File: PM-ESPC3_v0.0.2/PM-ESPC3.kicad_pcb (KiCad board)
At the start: 2 copper layers, 30.5 x 55.9 mm, 15 parts, among them J1 U254-051T-4BH83-S1S, J2 PinHeader_01x13_P2.54_THT_str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, J3 PinHeader_01x01_P2.54_THT_str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, SW1 Button, SW2 Button, SW3 DIP_SW-3P-P2.54-THT-Top, U1 ESP32-C3-WROOM-02U-N4

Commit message: new PM-RQ8
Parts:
- added C4: 10uF, Capacitor_SMD:C_1206_3216Metric_Pad1.33x1.80mm_HandSolder, F.Cu at (85.2, 133.0)
- added C5: 22uF, Capacitor_SMD:C_1206_3216Metric_Pad1.33x1.80mm_HandSolder, F.Cu at (85.2, 122.9)
- added D1: B5819W, Diode_SMD:D_SOD-123, F.Cu at (75.0, 128.0)
- added D2: B5819W, Diode_SMD:D_SOD-123, F.Cu at (75.0, 133.0)
- added D3: 5A 9.8V 6V, Diode_SMD:D_SOD-323_HandSoldering, F.Cu at (80.1, 133.0)
- added D4: Green, LED_SMD:LED_1206_3216Metric_Pad1.42x1.75mm_HandSolder, F.Cu at (75.0, 122.9)
- added H1: MountingHole, MountingHole:MountingHole_2.2mm_M2, F.Cu at (87.0, 139.0)
- added H2: MountingHole, MountingHole:MountingHole_2.2mm_M2, F.Cu at (53.0, 147.0)
- added H3: MountingHole, MountingHole:MountingHole_2.2mm_M2, F.Cu at (87.0, 61.0)
- added H4: MountingHole, MountingHole:MountingHole_2.2mm_M2, F.Cu at (53.0, 53.0)
- added J4: R-RJ11R04P-A802, kicad_inventree_lib:R-RJ11R04P-A802, F.Cu at (62.0, 148.0)
- added J5: X10B25L08T, kicad_inventree_lib:X10B25L08T, F.Cu at (67.5, 70.0)
- added J6: X10B25L08T, kicad_inventree_lib:X10B25L08T, F.Cu at (67.5, 90.0)
- added J7: X10B25L08T, kicad_inventree_lib:X10B25L08T, F.Cu at (67.5, 130.0)
- added R5: 680R, Resistor_SMD:R_1206_3216Metric_Pad1.30x1.75mm_HandSolder, F.Cu at (80.1, 125.4)
- added U2: CJA1117B-3.3, Package_TO_SOT_SMD:SOT-89-3, F.Cu at (85.2, 127.9)
- J2: value PinHeader_01x13_P2.54_THT_straight -> X10B25L08T; footprint Connector_PinHeader_2.54mm:PinHeader_1x13_P2.54mm_Vertical -> kicad_inventree_lib:X10B25L08T; moved to F.Cu
- J3: value PinHeader_01x01_P2.54_THT_straight -> R-RJ11R04P-A802; footprint Connector_PinHeader_2.54mm:PinHeader_1x01_P2.54mm_Vertical -> kicad_inventree_lib:R-RJ11R04P-A802; moved to F.Cu
- SW3: moved to F.Cu
- moved J3 77.7 mm to (75.0, 148.0)
- moved SW2 60.0 mm to (87.7, 67.0), turned to -90 degrees
- moved SW1 56.1 mm to (82.6, 67.0), turned to -90 degrees
- moved C3 45.8 mm to (87.7, 77.1), turned to 90 degrees
- moved R4 42.7 mm to (72.5, 77.1), turned to 90 degrees
- moved C1 37.7 mm to (82.6, 77.1), turned to 90 degrees
- moved R8 36.8 mm to (87.7, 115.2), turned to 90 degrees
- moved C2 36.6 mm to (87.7, 84.8)
- moved R3 32.6 mm to (72.5, 84.8)
- moved J2 32.2 mm to (67.5, 110.0), turned to -90 degrees
- moved R1 31.7 mm to (82.6, 84.8)
- moved R2 29.8 mm to (77.5, 84.8), turned to -90 degrees
- moved J1 26.6 mm to (63.6, 55.1)
- moved SW3 18.3 mm to (71.2, 53.0), turned to 0 degrees
- moved U1 4.40 mm to (82.6, 100.0), turned to -90 degrees
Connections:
- C2 pad 2: /+3.3V -> +3.3V
- C3 pad 1: /+3.3V -> +3.3V
- J1 pad 1: unconnected-(J1-VBUS-Pad1) -> Net-(D1-A)
- J2 pad 1: unconnected-(J2-Pin_1-Pad1) -> +5V
- J2 pad 2: /GPIO2 -> +3.3V
- J2 pad 3: /GPIO3 -> unconnected-(J2-Pin_3-Pad3)
- J2 pad 4: /GPIO9 -> /MOSI
- J2 pad 5: /GPIO8 -> /MISO
- J2 pad 6: /GPIO7 -> /SCK
- J2 pad 7: /GPIO6 -> /CS2
- J2 pad 8: /GPIO5 -> GND
- J3 pad 1: GND -> Net-(D2-A)
- R1 pad 1: /+3.3V -> +3.3V
- R2 pad 1: /+3.3V -> +3.3V
- R2 pad 2: /GPIO8 -> /A1
- R3 pad 1: /+3.3V -> +3.3V
- R3 pad 2: /GPIO9 -> /A2
- R4 pad 1: /GPIO9 -> /A2
- R8 pad 1: /+3.3V -> +3.3V
- R8 pad 2: /GPIO2 -> /MISO
- SW3 pad 1: /A2 -> +3.3V
- SW3 pad 2: /A1 -> +3.3V
- SW3 pad 3: /A0 -> +3.3V
- SW3 pad 4: /+3.3V -> /A0
- SW3 pad 5: /+3.3V -> /A1
- SW3 pad 6: /+3.3V -> /A2
- U1 pad 1: /+3.3V -> +3.3V
- U1 pad 10: /A2 -> /CS0
- U1 pad 11: /A1 -> /CS1
- U1 pad 12: /A0 -> /CS2
- U1 pad 15: /GPIO3 -> /CS3
- U1 pad 16: /GPIO2 -> /MISO
- U1 pad 3: /GPIO4 -> unconnected-(U1-IO4-Pad3)
- U1 pad 4: /GPIO5 -> /MOSI
- U1 pad 5: /GPIO6 -> /SCK
- U1 pad 6: /GPIO7 -> /A0
- U1 pad 7: /GPIO8 -> /A1
- U1 pad 8: /GPIO9 -> /A2
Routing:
- net GND: track 19.9 -> 0.00 mm
- net /USB_D+: track 17.7 -> 0.00 mm
- net /USB_D-: track 17.6 -> 0.00 mm
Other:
- board size 30.5 x 55.9 mm -> 39.8 x 99.8 mm
- board text added: "1"
- board text added: "2"
- board text added: "4"
- board text added: "OFF"
- board text added: "ON"
- board text added: "SPI0"
- board text added: "SPI1"
- board text added: "SPI2"
- board text added: "SPI3"
- board text removed: "+3.3V"
- board text removed: "CS1"
- board text removed: "CS2"
- board text removed: "GND"
- board text removed: "GPIO4"
- board text removed: "GPIO5"
- board text removed: "GPIO6"
- board text removed: "MISO"
- board text removed: "MOSI"
- board text removed: "SCK"
- board text removed: "SCL"
- board text removed: "SDA"

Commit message: update
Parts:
- removed D4: Green, LED_SMD:LED_1206_3216Metric_Pad1.42x1.75mm_HandSolder
- removed J7: X10B25L08T, kicad_inventree_lib:X10B25L08T
- removed R5: 680R, Resistor_SMD:R_1206_3216Metric_Pad1.30x1.75mm_HandSolder
- added J8: AFA07-S10FCC-00, kicad_inventree_lib:CONN10_AFA07-S10_JUS, F.Cu at (63.0, 70.0)
- added R6: 10k, Resistor_SMD:R_1206_3216Metric_Pad1.30x1.75mm_HandSolder, F.Cu at (74.5, 66.0)
- added R7: 330R, Resistor_SMD:R_1206_3216Metric_Pad1.30x1.75mm_HandSolder, F.Cu at (72.5, 115.2)
- J2, J5, J6: value X10B25L08T -> AFA07-S10FCC-00; footprint kicad_inventree_lib:X10B25L08T -> kicad_inventree_lib:CONN10_AFA07-S10_JUS
- moved J6 40.2 mm to (63.0, 130.0)
- moved J5 20.5 mm to (63.0, 90.0)
- moved J2 4.47 mm to (63.0, 110.0)
- moved J4 0.50 mm to (61.7, 147.6)
- moved J3 0.38 mm to (75.0, 147.6)
- moved J1 0.37 mm to (63.8, 55.4)
- moved U1 0.30 mm to (82.3, 100.1)
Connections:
- J2 pad 4: /MOSI -> unconnected-(J2-Pin_4-Pad4)
- J2 pad 5: /MISO -> unconnected-(J2-Pin_5-Pad5)
- J2 pad 6: /SCK -> unconnected-(J2-Pin_6-Pad6)
- J2 pad 7: /CS2 -> unconnected-(J2-Pin_7-Pad7)
- J2 pad 8: GND -> unconnected-(J2-Pin_8-Pad8)
- J5 pad 1: +5V -> unconnected-(J5-Pin_1-Pad1)
- J5 pad 2: +3.3V -> Net-(J5-Pin_2)
- J5 pad 3: unconnected-(J5-Pin_3-Pad3) -> +3.3V
- J5 pad 4: /MOSI -> /LED0
- J5 pad 5: /MISO -> /LED1
- J5 pad 6: /SCK -> /LED2
- J5 pad 7: /CS0 -> /LED3
- J5 pad 8: GND -> unconnected-(J5-Pin_8-Pad8)
- J6 pad 4: /MOSI -> unconnected-(J6-Pin_4-Pad4)
- J6 pad 5: /MISO -> /MOSI
- J6 pad 6: /SCK -> /MISO
- J6 pad 7: /CS1 -> /SCK
- J6 pad 8: GND -> /CS1
- R2 pad 2: /A1 -> /MISO
- R3 pad 2: /A2 -> /CS0
- R4 pad 1: /A2 -> /CS0
- R8 pad 2: /MISO -> /CS1
- SW3 pad 1: +3.3V -> Net-(R6-Pad2)
- SW3 pad 2: +3.3V -> Net-(R6-Pad2)
- SW3 pad 3: +3.3V -> Net-(R6-Pad2)
- SW3 pad 4: /A0 -> /LED0
- SW3 pad 5: /A1 -> /MOSI
- SW3 pad 6: /A2 -> /SCK
- U1 pad 10: /CS0 -> /LED3
- U1 pad 11: /CS1 -> /LED2
- U1 pad 12: /CS2 -> /LED1
- U1 pad 15: /CS3 -> /INT1
- U1 pad 16: /MISO -> /CS1
- U1 pad 3: unconnected-(U1-IO4-Pad3) -> /LED0
- U1 pad 6: /A0 -> /INT0
- U1 pad 7: /A1 -> /MISO
- U1 pad 8: /A2 -> /CS0
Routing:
- removed copper zone on F.Cu, net GND
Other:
- outline, holes or cut-outs redrawn
- board text added: "LED8"
- board text added: "Spare"
- board text removed: "SPI2"
- board text removed: "SPI3"

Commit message: update
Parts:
- removed SW3: DIP_SW-3P-P2.54-THT-Top, kicad_inventree_lib:SW_DIP_SPSTx03_Slide_9.78x9.8mm_W7.62mm_P2.54mm
- added SW4: DIP 3 pos, kicad_inventree_lib:DA03BLP, F.Cu at (77.5, 61.7)
- moved U1 5.90 mm to (76.5, 100.1)
- moved R6 4.04 mm to (72.5, 69.5)
- moved J2 2.00 mm to (61.0, 110.0)
- moved J5 2.00 mm to (61.0, 90.0)
- moved J6 2.00 mm to (61.0, 130.0)
- moved J8 2.00 mm to (61.0, 70.0)
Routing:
- net Net-(D2-A): track 0.00 -> 15.0 mm
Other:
- outline, holes or cut-outs redrawn
- board text removed: "OFF"
- board text removed: "ON"

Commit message: update
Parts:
- added U3: MAX3485, Package_SO:SOIC-8_3.9x4.9mm_P1.27mm, F.Cu at (80.1, 115.2)

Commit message: update
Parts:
- added R5: 10k, Resistor_SMD:R_1206_3216Metric_Pad1.30x1.75mm_HandSolder, F.Cu at (72.5, 115.2)
- added R9: 10k, Resistor_SMD:R_1206_3216Metric_Pad1.30x1.75mm_HandSolder, F.Cu at (82.6, 115.2)
- moved R7 10.8 mm to (80.1, 122.9)
- moved U3 10.8 mm to (72.5, 122.9), turned to -90 degrees
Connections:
- J2 pad 7: unconnected-(J2-Pin_7-Pad7) -> /SDA
- J2 pad 8: unconnected-(J2-Pin_8-Pad8) -> /SCL
- J2 pad 9: unconnected-(J2-Pin_9-Pad9) -> /INT
- J6 pad 4: unconnected-(J6-Pin_4-Pad4) -> /MOSI
- J6 pad 5: /MOSI -> /MISO
- J6 pad 6: /MISO -> /SCK
- J6 pad 7: /SCK -> /CS2
- J6 pad 8: /CS1 -> /CS3
- J8 pad 4: unconnected-(J8-Pin_4-Pad4) -> /MOSI
- J8 pad 5: /MOSI -> /MISO
- J8 pad 6: /MISO -> /SCK
- J8 pad 7: /SCK -> /CS0
- J8 pad 8: /CS0 -> /CS1
- J8 pad 9: /INT0 -> /INT
- R2 pad 2: /MISO -> /CS0
- R3 pad 2: /CS0 -> /CS1
- R4 pad 1: /CS0 -> /CS1
- R8 pad 2: /CS1 -> /CS2
- U1 pad 10: /LED3 -> /UART_DIR
- U1 pad 11: /LED2 -> /UART_RX
- U1 pad 12: /LED1 -> /UART_TX
- U1 pad 15: /INT1 -> /CS3
- U1 pad 16: /CS1 -> /CS2
- U1 pad 3: /LED0 -> /MOSI
- U1 pad 4: /MOSI -> /MISO
- U1 pad 6: /INT0 -> /INT
- U1 pad 7: /MISO -> /CS0
- U1 pad 8: /CS0 -> /CS1
- U3 pad 1: unconnected-(U3-RO-Pad1) -> /UART_RX
- U3 pad 2: unconnected-(U3-~{RE}-Pad2) -> /UART_DIR
- U3 pad 3: unconnected-(U3-DE-Pad3) -> /UART_DIR
- U3 pad 4: unconnected-(U3-DI-Pad4) -> /UART_TX
- U3 pad 6: unconnected-(U3-A-Pad6) -> /A
- U3 pad 7: unconnected-(U3-B-Pad7) -> /B
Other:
- board text added: "I2C"
- board text added: "SPI0,SPI1"
- board text added: "SPI2, SPI3"
- board text removed: "SPI0"
- board text removed: "SPI1"
- board text removed: "Spare"

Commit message: PM-Debug
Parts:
- removed J3, J4: R-RJ11R04P-A802, kicad_inventree_lib:R-RJ11R04P-A802
- removed J6: AFA07-S10FCC-00, kicad_inventree_lib:CONN10_AFA07-S10_JUS
- added C10: 10uF, Capacitor_SMD:C_1206_3216Metric_Pad1.33x1.80mm_HandSolder, F.Cu at (59.8, 120.3)
- added C11: 10uF, Capacitor_SMD:C_1206_3216Metric_Pad1.33x1.80mm_HandSolder, F.Cu at (59.8, 133.0)
- added C6: 100nF, Capacitor_SMD:C_1206_3216Metric_Pad1.33x1.80mm_HandSolder, F.Cu at (80.1, 125.4)
- added C7: 10uF, Capacitor_SMD:C_1206_3216Metric_Pad1.33x1.80mm_HandSolder, F.Cu at (80.1, 133.0)
- added C8: 100nF, Capacitor_SMD:C_1206_3216Metric_Pad1.33x1.80mm_HandSolder, F.Cu at (59.8, 125.4)
- added C9: 10uF, Capacitor_SMD:C_1206_3216Metric_Pad1.33x1.80mm_HandSolder, F.Cu at (80.1, 120.3)
- added J7: ~, kicad_inventree_lib:HC-WK88-H16-1X2-DB, F.Cu at (67.7, 139.9)
- added JP1: SolderJumper_2_Open, Jumper:SolderJumper-2_P1.3mm_Open_RoundedPad1.0x1.5mm, B.Cu at (69.9, 125.4)
- added JP2: SolderJumper_2_Open, Jumper:SolderJumper-2_P1.3mm_Open_RoundedPad1.0x1.5mm, B.Cu at (69.9, 120.3)
- added JP3: SolderJumper_2_Open, Jumper:SolderJumper-2_P1.3mm_Open_RoundedPad1.0x1.5mm, B.Cu at (69.9, 122.9)
- added JP4: SolderJumper_2_Open, Jumper:SolderJumper-2_P1.3mm_Open_RoundedPad1.0x1.5mm, B.Cu at (69.9, 127.9)
- added JP5: SolderJumper_2_Open, Jumper:SolderJumper-2_P1.3mm_Open_RoundedPad1.0x1.5mm, B.Cu at (69.9, 117.8)
- added JP6: SolderJumper_2_Open, Jumper:SolderJumper-2_P1.3mm_Open_RoundedPad1.0x1.5mm, B.Cu at (69.9, 130.5)
- added PS1: B0505S-1WR3, kicad_inventree_lib:B0505S1WR3, F.Cu at (66.1, 134.8)
- added R10: 3k3, Resistor_SMD:R_1206_3216Metric_Pad1.30x1.75mm_HandSolder, F.Cu at (64.8, 89.8)
- added R11: 3k3, Resistor_SMD:R_1206_3216Metric_Pad1.30x1.75mm_HandSolder, F.Cu at (64.8, 84.8)
- added REF**: MountingHole_3.2mm_M3, MountingHole:MountingHole_3.2mm_M3, F.Cu at (86.0, 68.0)
- added U4: CA-IS3641HW, kicad_inventree_lib:SOIC16-WBW_CLG-M, F.Cu at (69.9, 122.9)
- moved SW1 27.4 mm to (57.2, 56.8)
- moved SW2 27.4 mm to (62.3, 56.8)
- moved R7 25.4 mm to (64.8, 102.5), turned to 180 degrees
- moved C4 24.1 mm to (77.5, 110.2), turned to 90 degrees
- moved D3 24.1 mm to (72.5, 110.2)
- moved D1 21.7 mm to (67.4, 107.6)
- moved D2 21.7 mm to (67.4, 112.7)
- moved R1 21.7 mm to (75.0, 64.4), turned to -90 degrees
- moved J2 21.5 mm to (53.0, 90.0)
- moved J5 21.5 mm to (53.0, 110.0)
- moved J1 20.1 mm to (83.9, 55.4)
- moved R5 19.3 mm to (54.7, 122.9), turned to 180 degrees
- moved U3 19.3 mm to (54.7, 130.5)
- moved U2 18.0 mm to (82.6, 110.2), turned to 0 degrees
- moved C1 18.0 mm to (69.9, 64.4)
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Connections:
- D2 pad 2: Net-(D2-A) -> +5V_BUS
- J5 pad 4: /LED0 -> /USB_D-
- J5 pad 5: /LED1 -> /USB_D+
- J5 pad 6: /LED2 -> unconnected-(J5-Pin_6-Pad6)
- J5 pad 7: /LED3 -> unconnected-(J5-Pin_7-Pad7)
- J5 pad 8: unconnected-(J5-Pin_8-Pad8) -> /UART_RX
- J5 pad 9: unconnected-(J5-Pin_9-Pad9) -> /UART_TX
- J8 pad 3: unconnected-(J8-Pin_3-Pad3) -> /MOSI
- J8 pad 4: /MOSI -> /MISO
- J8 pad 5: /MISO -> /SCK
- J8 pad 6: /SCK -> /CS0
- J8 pad 7: /CS0 -> /CS1
- J8 pad 8: /CS1 -> /CS2
- J8 pad 9: /INT -> /CS3
- R5 pad 1: /UART_DIR -> /UART_DIR_ISO
- R5 pad 2: GND -> GND_ISO
- SW4 pad 1: /SCK -> /MOSI
- SW4 pad 2: /MOSI -> /MISO
- SW4 pad 3: /LED0 -> /SCK
- U3 pad 1: /UART_RX -> /UART_RX_ISO
- U3 pad 2: /UART_DIR -> /UART_DIR_ISO
- U3 pad 3: /UART_DIR -> /UART_DIR_ISO
- U3 pad 4: /UART_TX -> /UART_TX_ISO
- U3 pad 5: GND -> GND_ISO
- U3 pad 8: +3.3V -> +3.3V_ISO
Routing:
- net +3.3V: track 0.00 -> 208.2 mm, vias 0 -> 1
- net /USB_D+: track 0.00 -> 134.0 mm
- net /USB_D-: track 0.00 -> 74.5 mm, vias 0 -> 2
- net +5V: track 0.00 -> 72.5 mm
- net Net-(D1-A): track 0.00 -> 65.9 mm, vias 0 -> 2
- net /UART_TX: track 0.00 -> 60.2 mm, vias 0 -> 2
- net /MISO: track 0.00 -> 52.0 mm, vias 0 -> 1
- net /UART_RX: track 0.00 -> 50.8 mm, vias 0 -> 2
- net /CS2: track 0.00 -> 48.6 mm, vias 0 -> 2
- net /CS3: track 0.00 -> 47.3 mm, vias 0 -> 2
- net GND: track 0.00 -> 44.7 mm, vias 0 -> 20
- net +5V_ISO: track 0.00 -> 44.6 mm
- net /MOSI: track 0.00 -> 42.8 mm, vias 0 -> 2
- net /SCK: track 0.00 -> 40.5 mm
- net /A: track 0.00 -> 37.9 mm
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- added copper zone on B.Cu, net GND_ISO
- added copper zone on F.Cu, net GND_ISO
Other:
- outline, holes or cut-outs redrawn
- board text added: "SPI"
- board text removed: "SPI0,SPI1"
- board text removed: "SPI2, SPI3"

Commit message: main
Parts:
- removed REF**: MountingHole_3.2mm_M3, MountingHole:MountingHole_3.2mm_M3
- moved J7 3.61 mm to (64.7, 137.9)
- moved H2 2.83 mm to (51.0, 145.0)
- moved H4 2.83 mm to (51.0, 55.0)
- moved J2 2.00 mm to (51.0, 90.0)
- moved J5 2.00 mm to (51.0, 110.0)
- moved J8 2.00 mm to (51.0, 70.0)
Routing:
- net +3.3V: track 208.2 -> 0.00 mm, vias 1 -> 0
- net /USB_D+: track 134.0 -> 0.00 mm
- net /USB_D-: track 74.5 -> 0.00 mm, vias 2 -> 0
- net +5V: track 72.5 -> 0.00 mm
- net Net-(D1-A): track 65.9 -> 0.00 mm, vias 2 -> 0
- net /UART_TX: track 60.2 -> 0.00 mm, vias 2 -> 0
- net /MISO: track 52.0 -> 0.00 mm, vias 1 -> 0
- net /UART_RX: track 50.8 -> 0.00 mm, vias 2 -> 0
- net /CS2: track 48.6 -> 0.00 mm, vias 2 -> 0
- net /CS3: track 47.3 -> 0.00 mm, vias 2 -> 0
- net GND: track 44.7 -> 0.00 mm, vias 20 -> 0
- net +5V_ISO: track 44.6 -> 0.00 mm
- net /MOSI: track 42.8 -> 0.00 mm, vias 2 -> 0
- net /SCK: track 40.5 -> 0.00 mm
- net /A: track 37.9 -> 0.00 mm
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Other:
- board size 39.8 x 99.8 mm -> 41.8 x 95.8 mm

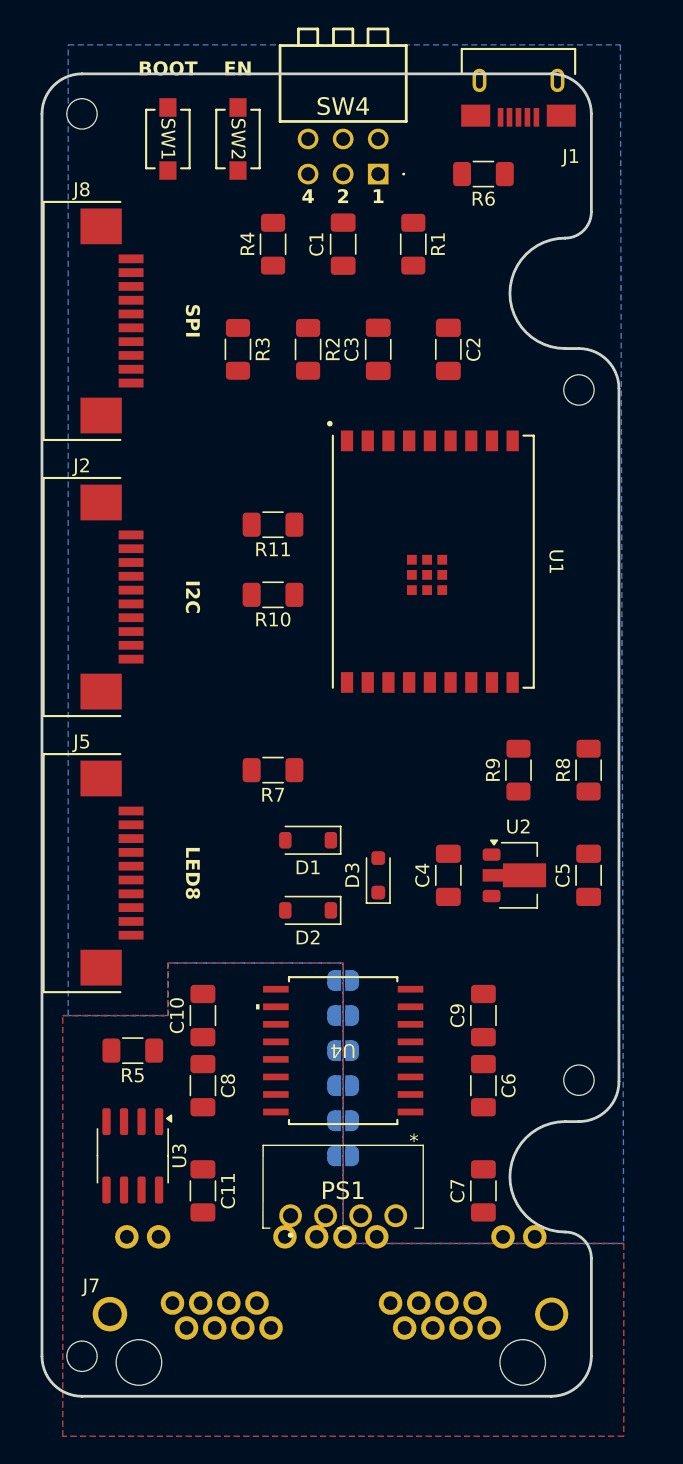
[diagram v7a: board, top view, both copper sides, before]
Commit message: update new size
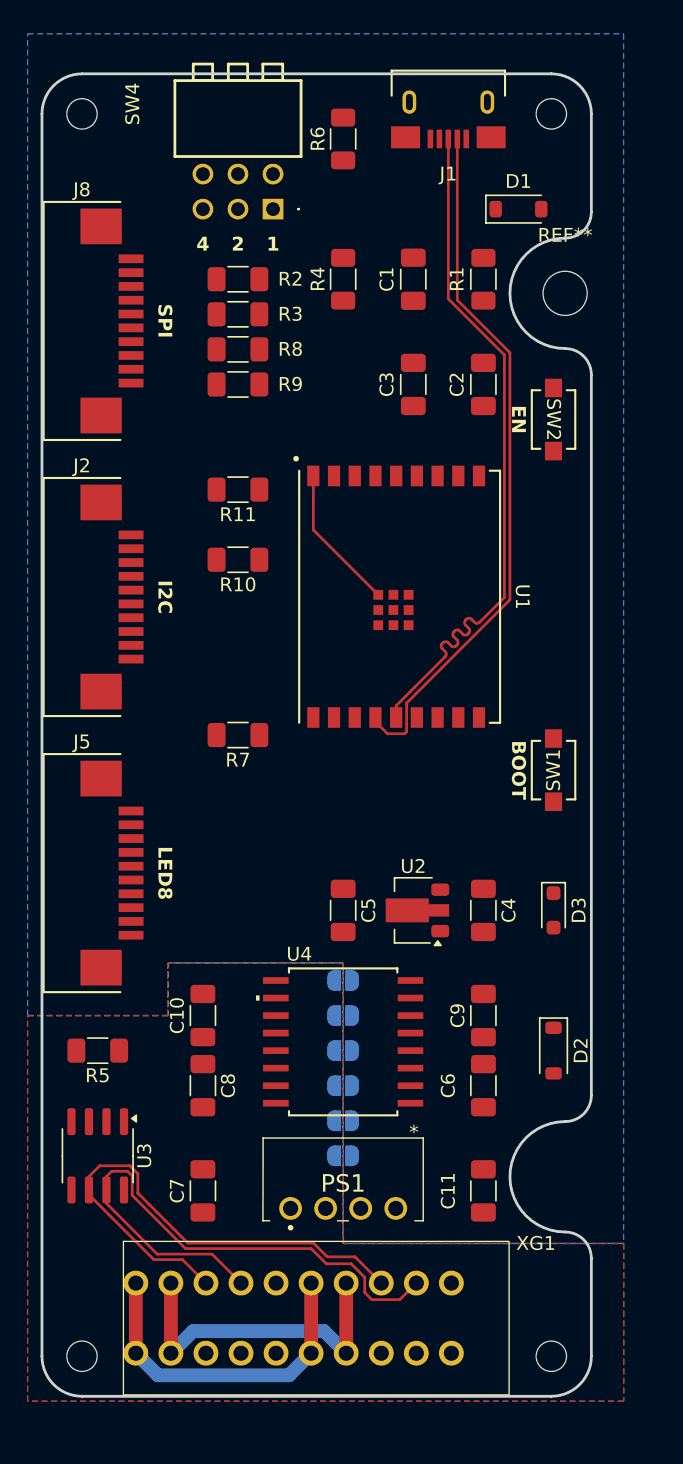
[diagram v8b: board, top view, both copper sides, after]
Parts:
- removed J7: ~, kicad_inventree_lib:HC-WK88-H16-1X2-DB
- added REF**: MountingHole_3.2mm_M3, MountingHole:MountingHole_3.2mm_M3, F.Cu at (86.0, 68.0)
- added XG1: DG141R-2.54-10P, kicad_inventree_lib:DG141R-2.54-10P, F.Cu at (54.0, 147.8)
- moved SW1 53.6 mm to (85.2, 102.5), turned to 90 degrees
- moved D1 48.2 mm to (82.6, 61.9), turned to 0 degrees
- moved R8 39.7 mm to (62.3, 72.1), turned to 180 degrees
- moved R9 34.5 mm to (62.3, 74.6), turned to 0 degrees
- moved SW2 30.6 mm to (85.2, 77.1)
- moved D2 20.5 mm to (85.2, 122.9), turned to -90 degrees
- moved C11 20.3 mm to (80.1, 133.0)
- moved C7 20.3 mm to (59.8, 133.0)
- moved H1 20.1 mm to (85.0, 145.0)
- moved H3 20.1 mm to (85.0, 55.0)
- moved C5 18.0 mm to (69.9, 112.7), turned to -90 degrees
- moved D3 13.0 mm to (85.2, 112.7), turned to -90 degrees
- moved R6 10.5 mm to (69.9, 56.8), turned to 90 degrees
- moved U2 8.03 mm to (75.0, 112.7), turned to 180 degrees
- moved SW4 8.03 mm to (64.8, 61.9)
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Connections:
- C11 pad 1: +5V_ISO -> Net-(D2-A)
- C11 pad 2: GND_ISO -> GND
- C7 pad 1: +5V_BUS -> +5V_ISO
- C7 pad 2: GND -> GND_ISO
- D2 pad 2: +5V_BUS -> Net-(D2-A)
- JP5 pad 1: GND -> GND_ISO
- JP5 pad 2: GND_ISO -> GND
- JP6 pad 1: +5V_BUS -> +5V_ISO
- JP6 pad 2: +5V_ISO -> Net-(D2-A)
- PS1 pad 1: GND_ISO -> +5V_ISO
- PS1 pad 2: +5V_ISO -> GND_ISO
- PS1 pad 4: +5V_BUS -> Net-(D2-A)
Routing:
- net /USB_D-: track 0.00 -> 50.6 mm
- net /USB_D+: track 0.00 -> 50.4 mm
- net /B: track 0.00 -> 42.5 mm
- net /A: track 0.00 -> 38.3 mm
- net GND_ISO: track 0.00 -> 24.2 mm
- net +5V_ISO: track 0.00 -> 24.2 mm
- net GND: track 0.00 -> 10.6 mm
- added copper zone on B.Cu, net PE
- added copper zone on F.Cu, net PE
- removed copper zone on B.Cu, net GND_ISO
- removed copper zone on F.Cu, net GND_ISO
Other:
- board size 41.8 x 95.8 mm -> 39.8 x 95.8 mm
